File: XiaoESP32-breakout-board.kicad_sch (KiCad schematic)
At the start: 2 parts

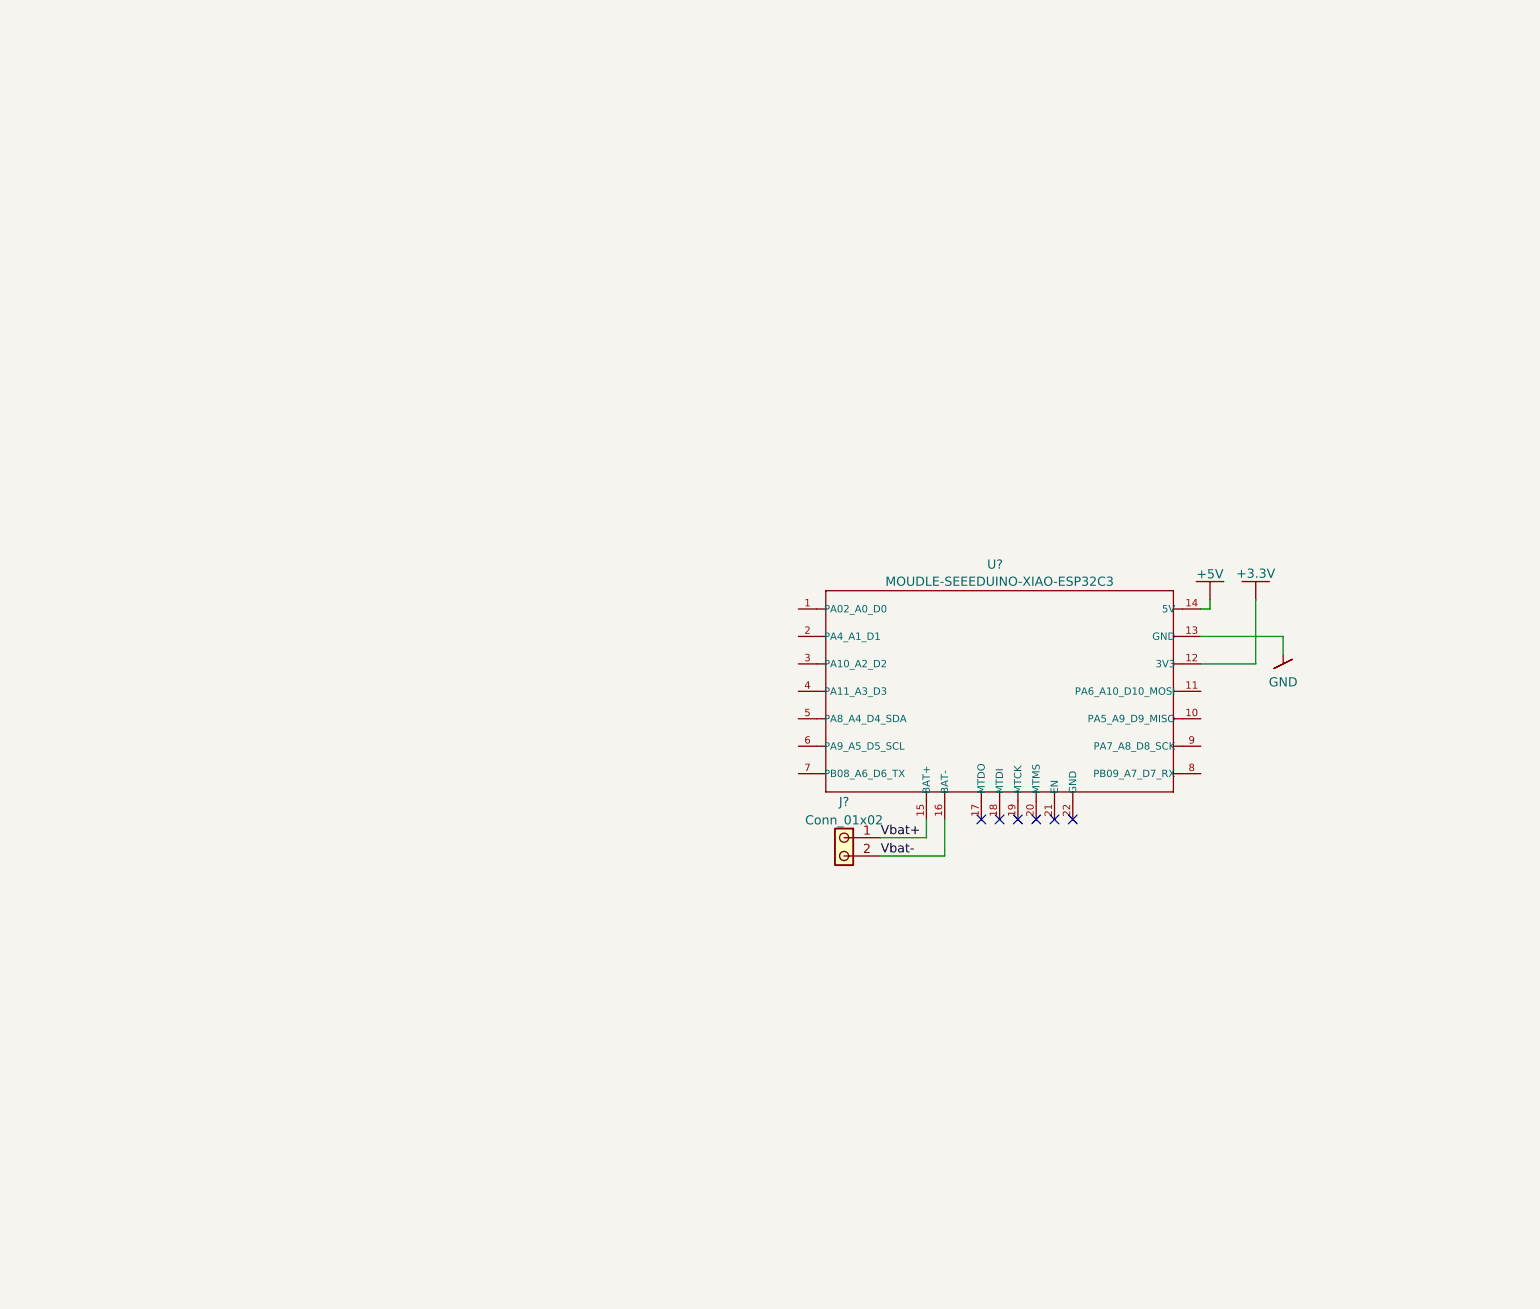
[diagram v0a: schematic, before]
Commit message: Add general schematic components
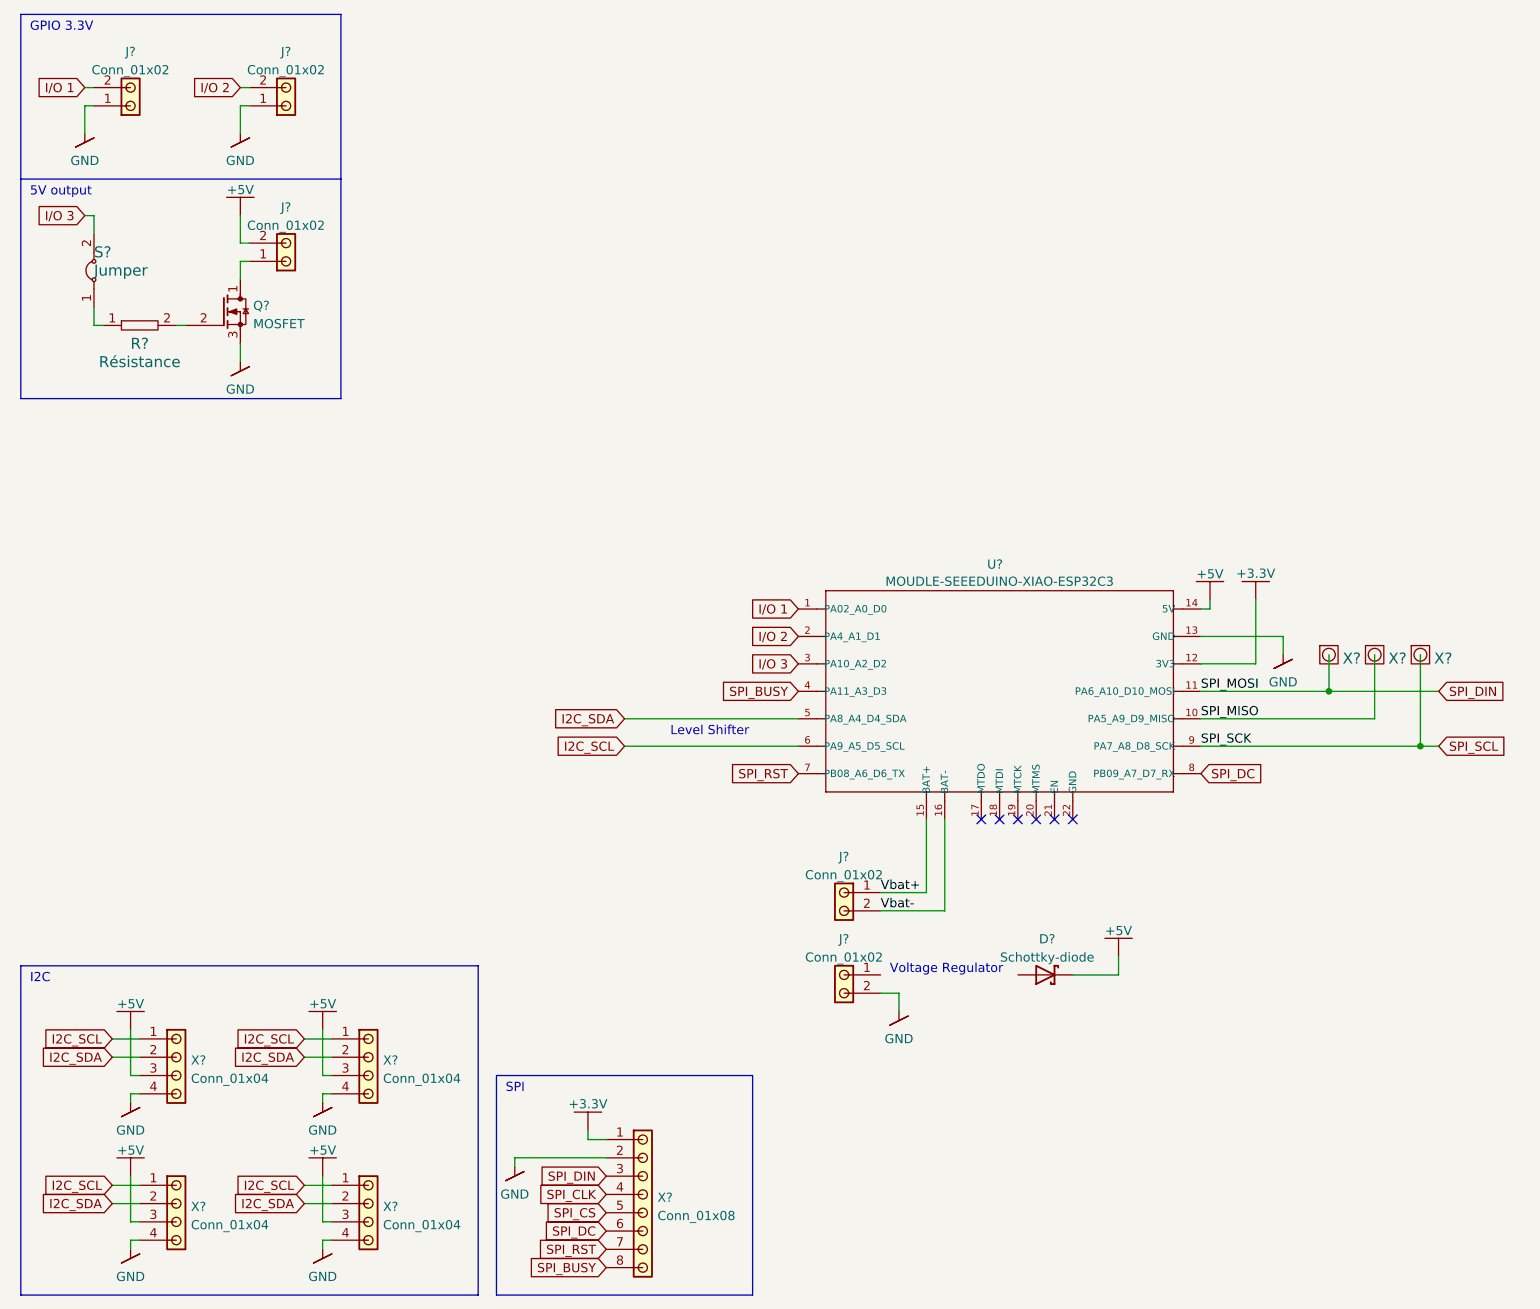
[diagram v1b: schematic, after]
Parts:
- added D?: Schottky-diode, Diode_THT:D_DO-41_SOD81_P10.16mm_Horizontal, symbol XiaoESP32-breakout-board:Schottky-diode
- added J? (x4): Conn_01x02, symbol XiaoESP32-breakout-board:Conn_01x02
- added Q?: MOSFET, symbol XiaoESP32-breakout-board:MOSFET
- added R?: Résistance, symbol XiaoESP32-breakout-board:Résistance
- added S?: Jumper, symbol XiaoESP32-breakout-board:Jumper
- added X? (x3): TestPoint, symbol XiaoESP32-breakout-board:TestPoint
- added X? (x4): Conn_01x04, symbol XiaoESP32-breakout-board:Conn_01x04
- added X?: Conn_01x08, symbol XiaoESP32-breakout-board:Conn_01x08
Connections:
- net +3.3V: now also X?.1 (Pin_1)
- net +5V: now also D?.1 (K), J?.2 (Pin_2), X?.3 (Pin_3), X?.3 (Pin_3), X?.3 (Pin_3), X?.3 (Pin_3)
- net GND: now also J?.1 (Pin_1), J?.1 (Pin_1), J?.2 (Pin_2), Q?.3 (S), X?.2 (Pin_2), X?.4 (Pin_4), X?.4 (Pin_4), X?.4 (Pin_4), X?.4 (Pin_4)
- net I/O 1: now reaches U?.1 (PA02_A0_D0)
- net I/O 1: now also J?.2 (Pin_2)
- net SPI_MISO: now reaches U?.10 (PA5_A9_D9_MISO)
- net SPI_MISO: now also X?.1
- net SPI_DIN: now reaches U?.11 (PA6_A10_D10_MOSI)
- net SPI_DIN: now also X?.1, X?.3 (Pin_3)
- net I/O 2: now reaches U?.2 (PA4_A1_D1)
- net I/O 2: now also J?.2 (Pin_2)
- net I/O 3: now reaches U?.3 (PA10_A2_D2)
- net I/O 3: now also S?.2
- net SPI_BUSY: now reaches U?.4 (PA11_A3_D3)
- net SPI_BUSY: now also X?.8 (Pin_8)
- net I2C_SDA: now reaches U?.5 (PA8_A4_D4_SDA)
- net I2C_SDA: now also X?.2 (Pin_2), X?.2 (Pin_2), X?.2 (Pin_2), X?.2 (Pin_2)
- net I2C_SCL: now reaches U?.6 (PA9_A5_D5_SCL)
- net I2C_SCL: now also X?.1 (Pin_1), X?.1 (Pin_1), X?.1 (Pin_1), X?.1 (Pin_1)
- net SPI_RST: now reaches U?.7 (PB08_A6_D6_TX)
- net SPI_RST: now also X?.7 (Pin_7)
- net SPI_DC: now reaches U?.8 (PB09_A7_D7_RX)
- net SPI_DC: now also X?.6 (Pin_6)
- net SPI_SCL: now reaches U?.9 (PA7_A8_D8_SCK)
- net SPI_SCL: now also X?.1
- new net: R?.1, S?.1
- new net: Q?.2 (G), R?.2
- new net: J?.1 (Pin_1), Q?.1 (D)
- new net SPI_CLK: X?.4 (Pin_4)
- new net SPI_CS: X?.5 (Pin_5)
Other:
- note added: "5V output"
- note added: "GPIO 3.3V"
- note added: "I2C"
- note added: "Level Shifter"
- note added: "SPI"
- note added: "Voltage Regulator"
- moved on the sheet: J?

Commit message: Schematic update
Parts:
- added R2, R3, R4, R5: Résistance, symbol XiaoESP32-breakout-board:Résistance
- added U1: TCA9617B, symbol XiaoESP32-breakout-board:TCA9617B
- added U2: Voltage Regulator, symbol XiaoESP32-breakout-board:Voltage-Regulator
- gave numbers to parts that had none: 18
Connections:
- net +3.3V: now also R4.2, R5.2, U1. (VCCB)
- net +5V: now also R2.2, R3.2, U1. (VCCB)
- net GND: now also U1. (VCCB), U2.1 (GND)
- net I2C_SCL: now also R2.1, U1. (VCCB); no longer U3.6 (PA9_A5_D5_SCL)
- net I2C_SDA: now also R3.1, U1. (VCCB); no longer U3.5 (PA8_A4_D4_SDA)
- net at J5.1 (Pin_1): now also U2.4 (VI)
- net at D1.2 (A): now also U2.2 (VO), U2.3 (VO), U2.6 (VO), U2.7 (VO)
- new net: R5.1, U1. (VCCB), U3.6 (PA9_A5_D5_SCL)
- new net: R4.1, U1. (VCCB), U3.5 (PA8_A4_D4_SDA)
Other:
- note removed: "Level Shifter"
- note removed: "Voltage Regulator"
- moved on the sheet: D1
